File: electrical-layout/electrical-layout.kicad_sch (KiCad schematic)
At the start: 4 parts, among them K1 DNCLEV100, SW1 SW_Push, U1 Outdrive 5.0

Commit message: layout-2025: add cockpit page and schematic
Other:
- added sheet Cockpit (cockpit.kicad_sch)
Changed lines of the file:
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@@
 		(exclude_from_sim no)
 		(at 179.8975 44.7897 0)
-		(size 39.1775 21.2503)
+		(size 37.2725 9.8203)
 		(margins 0.9525 0.9525 0.9525 0.9525)
 		(stroke
@@
 			(project "electrical-layout"
 				(path "/3f5ae950-00dd-4aca-9f75-0d872ff9560e"
+					(page "3")
+				)
+			)
+		)
+	)
+	(sheet
+		(at 174.625 66.675)
+		(size 59.055 19.685)
+		(exclude_from_sim no)
+		(in_bom yes)
+		(on_board yes)
+		(dnp no)
+		(fields_autoplaced yes)
+		(stroke
+			(width 0.1524)
+			(type solid)
+		)
+		(fill
+			(color 0 0 0 0.0000)
+		)
+		(property "Sheetname" "Cockpit"
+			(at 174.625 65.9634 0)
+			(effects
+				(font
+					(size 1.27 1.27)
+				)
+				(justify left bottom)
+			)
+		)
+		(property "Sheetfile" "cockpit.kicad_sch"
+			(at 174.625 86.9446 0)
+			(effects
+				(font
+					(size 1.27 1.27)
+				)
+				(justify left top)
+			)
+		)
+		(instances
+			(project "electrical-layout"
+				(path "/3f5ae950-00dd-4aca-9f75-0d872ff9560e"
 					(page "2")
 				)
@@
 			(project "electrical-layout"
 				(path "/3f5ae950-00dd-4aca-9f75-0d872ff9560e"
-					(page "3")
-				)
-			)
+					(page "4")
+				)
+			)

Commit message: layout-2025: add h2 control page and schematic
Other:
- added sheet H2 Control (h2_control.kicad_sch)
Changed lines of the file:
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@@
+	)
+	(sheet
+		(at 178.435 111.76)
+		(size 60.96 20.955)
+		(exclude_from_sim no)
+		(in_bom yes)
+		(on_board yes)
+		(dnp no)
+		(fields_autoplaced yes)
+		(stroke
+			(width 0.1524)
+			(type solid)
+		)
+		(fill
+			(color 0 0 0 0.0000)
+		)
+		(property "Sheetname" "H2 Control"
+			(at 178.435 111.0484 0)
+			(effects
+				(font
+					(size 1.27 1.27)
+				)
+				(justify left bottom)
+			)
+		)
+		(property "Sheetfile" "h2_control.kicad_sch"
+			(at 178.435 133.2996 0)
+			(effects
+				(font
+					(size 1.27 1.27)
+				)
+				(justify left top)
+			)
+		)
+		(instances
+			(project "electrical-layout"
+				(path "/3f5ae950-00dd-4aca-9f75-0d872ff9560e"
+					(page "5")
+				)
+			)
+		)
 	)
 	(sheet

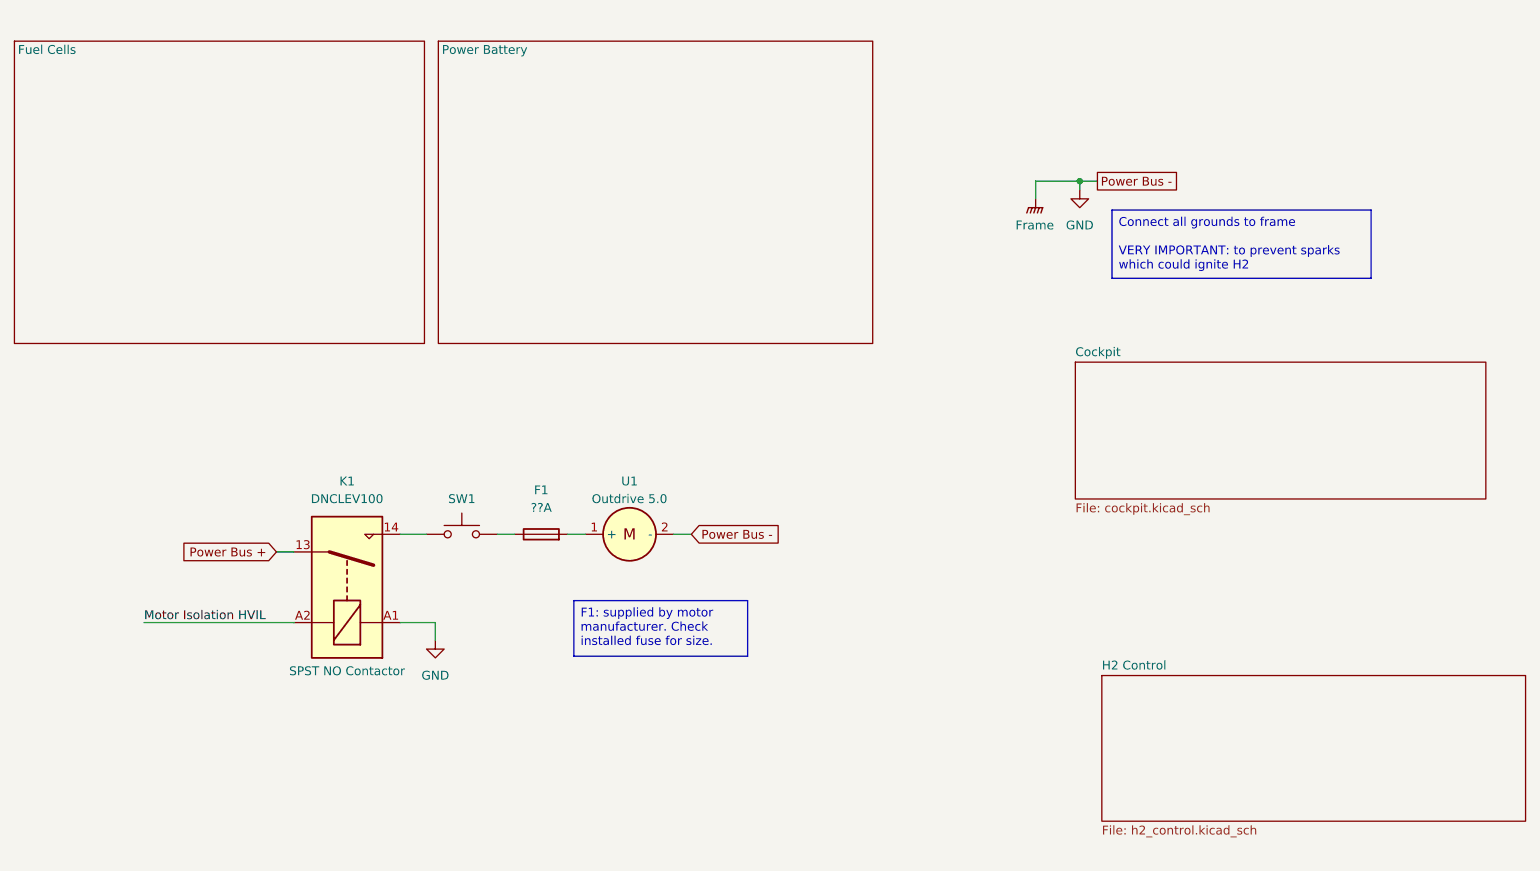
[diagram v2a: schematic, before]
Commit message: layout-2025: reorganize pages
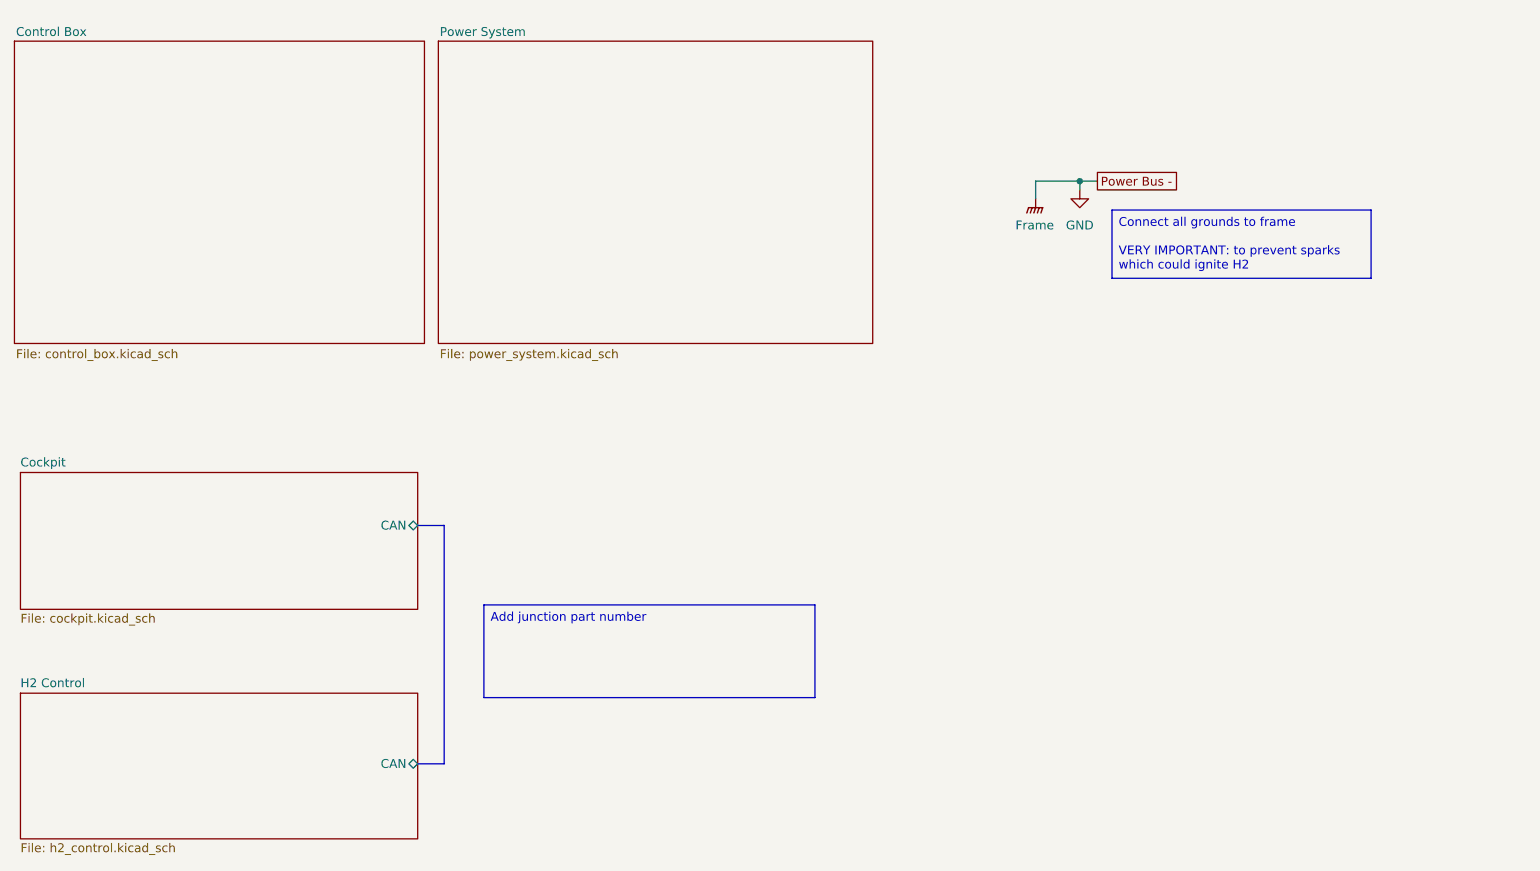
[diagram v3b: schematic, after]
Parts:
- removed F1: ??A, symbol Device:Fuse
- removed K1: DNCLEV100, symbol Relay:Relay_SPST-NO
- removed SW1: SW_Push, symbol Switch:SW_Push
- removed U1: Outdrive 5.0, symbol Exocet:Outboard_5.0
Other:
- sheet Fuel Cells renamed Control Box
- sheet Power Battery renamed Power System
- sheet Cockpit ports: added CAN; removed none
- sheet Control Box: file fuel_cells.kicad_sch -> control_box.kicad_sch
- sheet H2 Control ports: added CAN; removed none
- sheet Power System: file power_battery.kicad_sch -> power_system.kicad_sch

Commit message: layout-2025: add telemetry battery and pcb
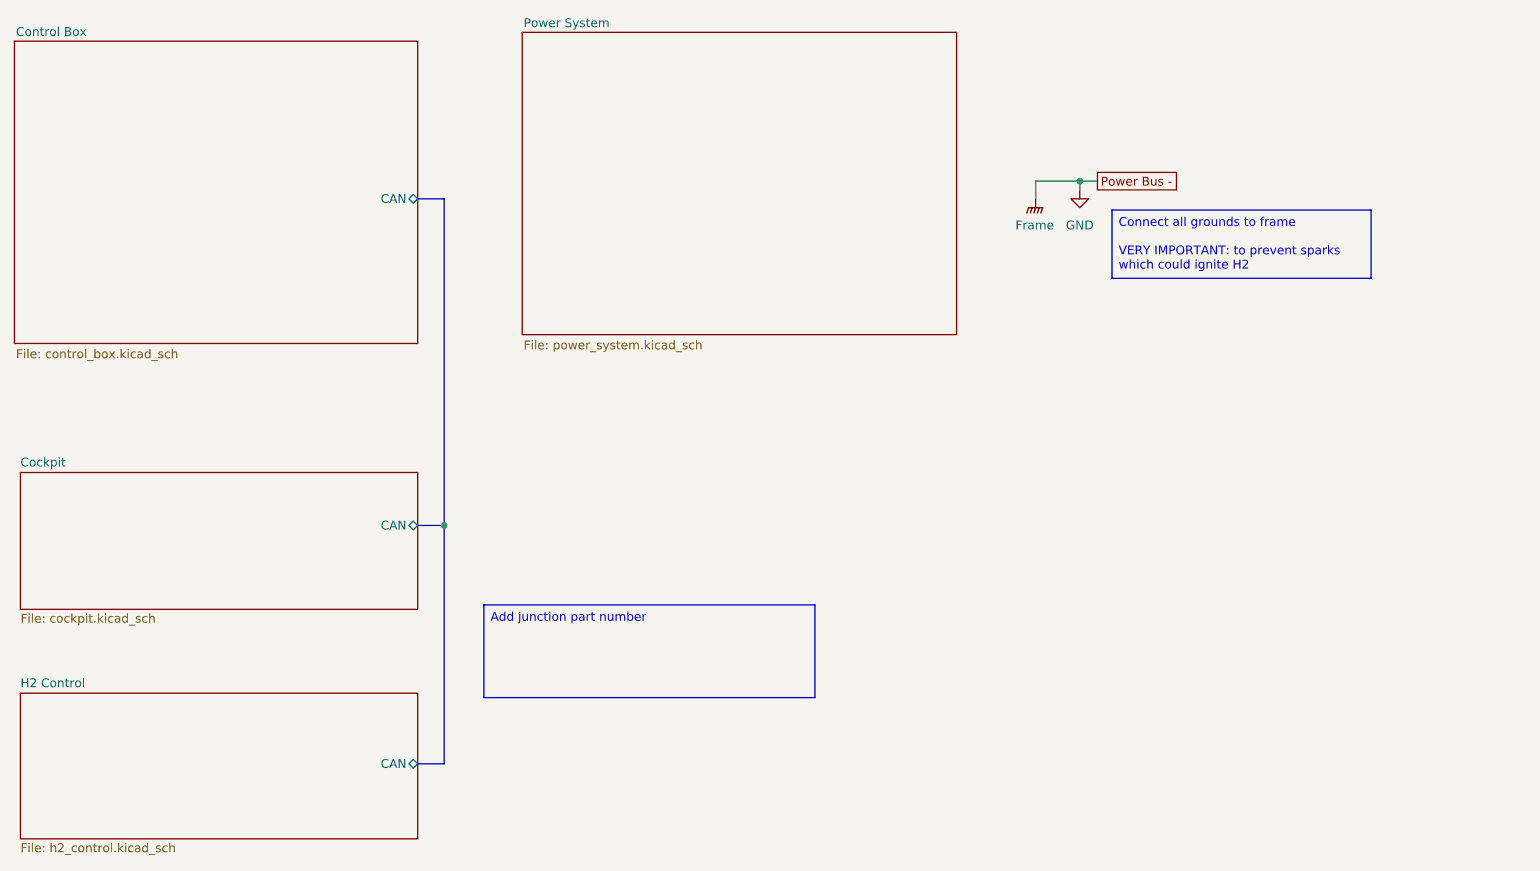
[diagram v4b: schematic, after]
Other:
- sheet Control Box ports: added CAN; removed none
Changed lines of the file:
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@@
 		(color 0 0 0 0)
 	)
+	(junction
+		(at 83.82 90.17)
+		(diameter 0)
+		(color 0 0 0 0)
+	)
+	(bus
+		(pts
+			(xy 80.01 43.18) (xy 83.82 43.18)
+		)
+		(stroke
+			(width 0)
+			(type default)
+		)
+	)
 	(wire
 		(pts
@@
 		(pts
 			(xy 83.82 90.17) (xy 83.82 124.46)
+		)
+		(stroke
+			(width 0)
+			(type default)
+		)
+	)
+	(bus
+		(pts
+			(xy 83.82 43.18) (xy 83.82 90.17)
 		)
 		(stroke
@@
 	(sheet
 		(at 21.9956 20.4959)
-		(size 58.9882 43.4913)
+		(size 58.0144 43.4913)
 		(exclude_from_sim no)
 		(in_bom yes)
@@
 				)
 				(justify left top)
+			)
+		)
+		(pin "CAN" bidirectional
+			(at 80.01 43.18 0)
+			(effects
+				(font
+					(size 1.27 1.27)
+				)
+				(justify right)
 			)
 		)
@@
 	)
 	(sheet
-		(at 82.9834 20.4959)
+		(at 95.0484 19.2259)
 		(size 62.4875 43.4913)
 		(exclude_from_sim no)
@@
 		)
 		(property "Sheetname" "Power System"
-			(at 83.185 18.415 0)
+			(at 95.25 17.145 0)
 			(effects
 				(font
@@
 		)
 		(property "Sheetfile" "power_system.kicad_sch"
-			(at 83.185 64.77 0)
-			(effects
-				(font
+			(at 95.25 63.5 0)
+			(effects
+				(font

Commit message: power-system: add DC-DC charger and temp. switches
This includes changes recommended to us during summer of 2025. Temporary
switch symbols have been used to indicate where to expect them, while
their internal circuit is not yet know and implemented. These will most
likely be replaced by some power transistors in the future.

A few control signals were added and are not yet connected to a control
board, but these shall be implemented on the power control PCB.
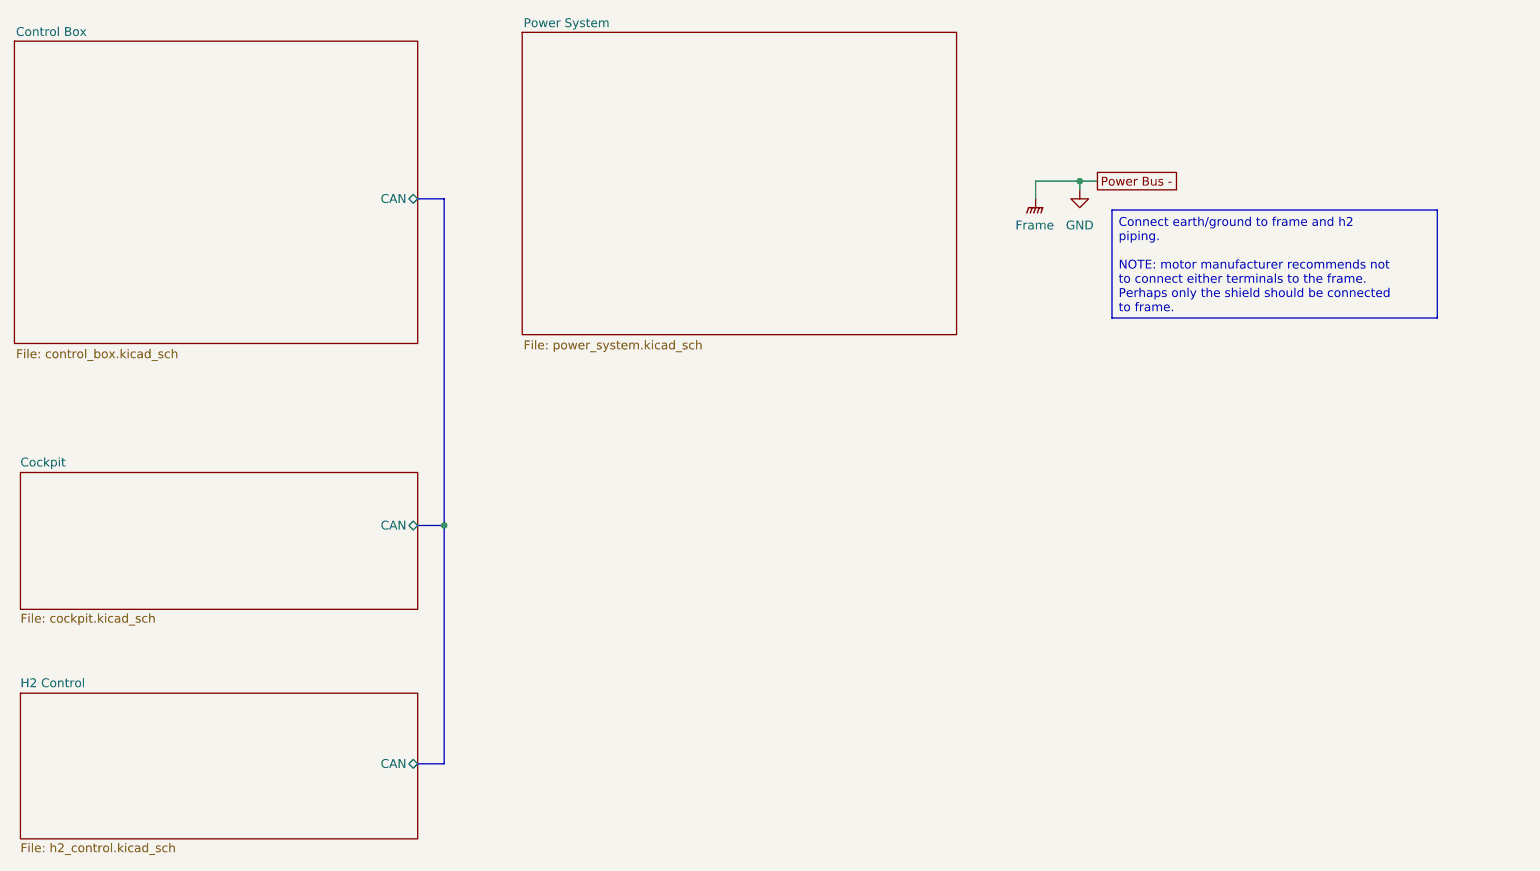
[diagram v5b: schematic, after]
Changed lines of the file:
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@@
 	(title_block
 		(title "Overview")
-		(date "2025-03-15")
-		(rev "v0.2.0")
+		(date "2025-09-06")
+		(rev "v0.3.0")
 	)
-	(text_box "Connect all grounds to frame\n\nVERY IMPORTANT: to prevent sparks which could ignite H2"
+	(text_box "Connect earth/ground to frame and h2 piping.\n\nNOTE: motor manufacturer recommends not to connect either terminals to the frame. Perhaps only the shield should be connected to frame."
 		(exclude_from_sim no)
 		(at 179.8975 44.7897 0)
-		(size 37.2725 9.8203)
+		(size 46.7975 15.5353)
 		(margins 0.9525 0.9525 0.9525 0.9525)
 		(stroke
-			(width 0)
-			(type solid)
-		)
-		(fill
-			(type none)
-		)
-		(effects
-			(font
-				(size 1.27 1.27)
-			)
-			(justify left top)
-		)
-	)
-	(text_box "Add junction part number"
-		(exclude_from_sim no)
-		(at 89.535 101.6 0)
-		(size 47.625 13.335)
-		(margins 0.9525 0.9525 0.9525 0.9525)
-		(stroke

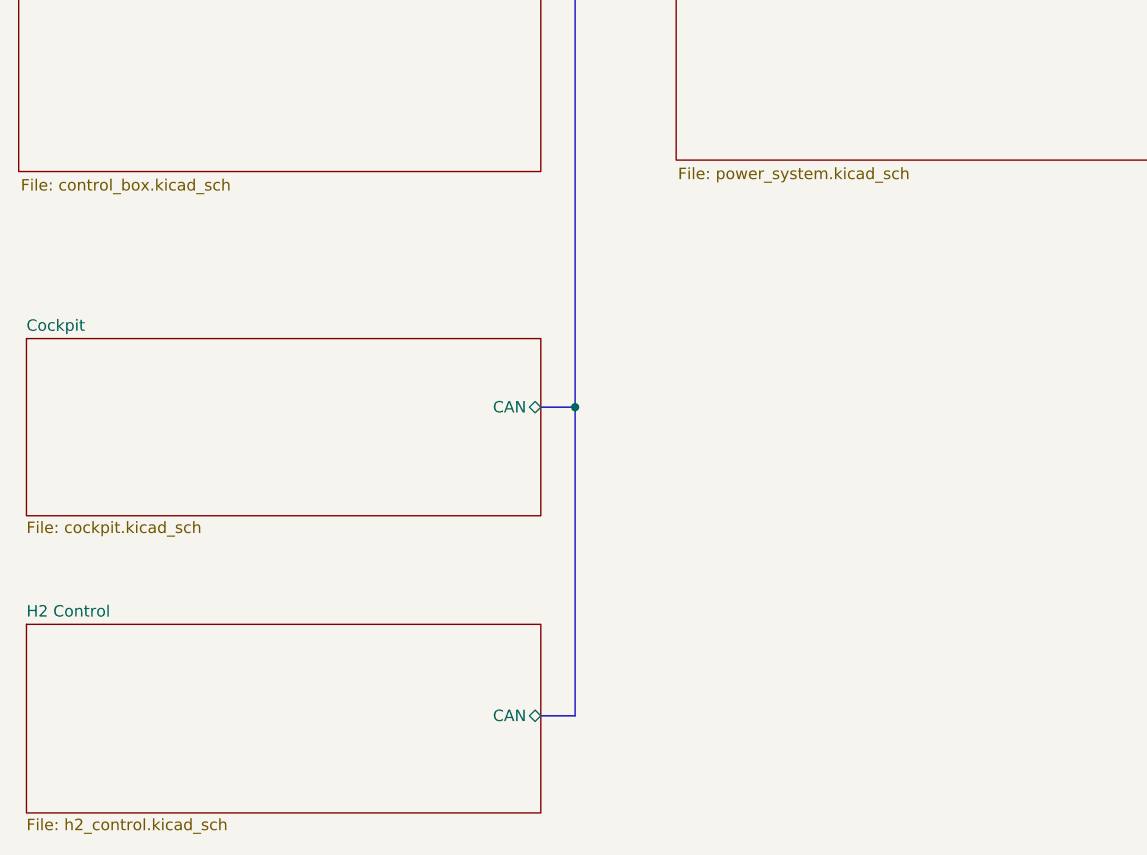
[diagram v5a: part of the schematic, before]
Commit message: layout-2025: change to version 3.0
A few changes were made for this new version:
- Version and dates were changed on all sheets
- Added a switch (temporary symbol) after the telemetry battery
- A few notes were removed, as these have either been resolved or
discussed somewhere else
- Changed battery symbol to multi-cell battery
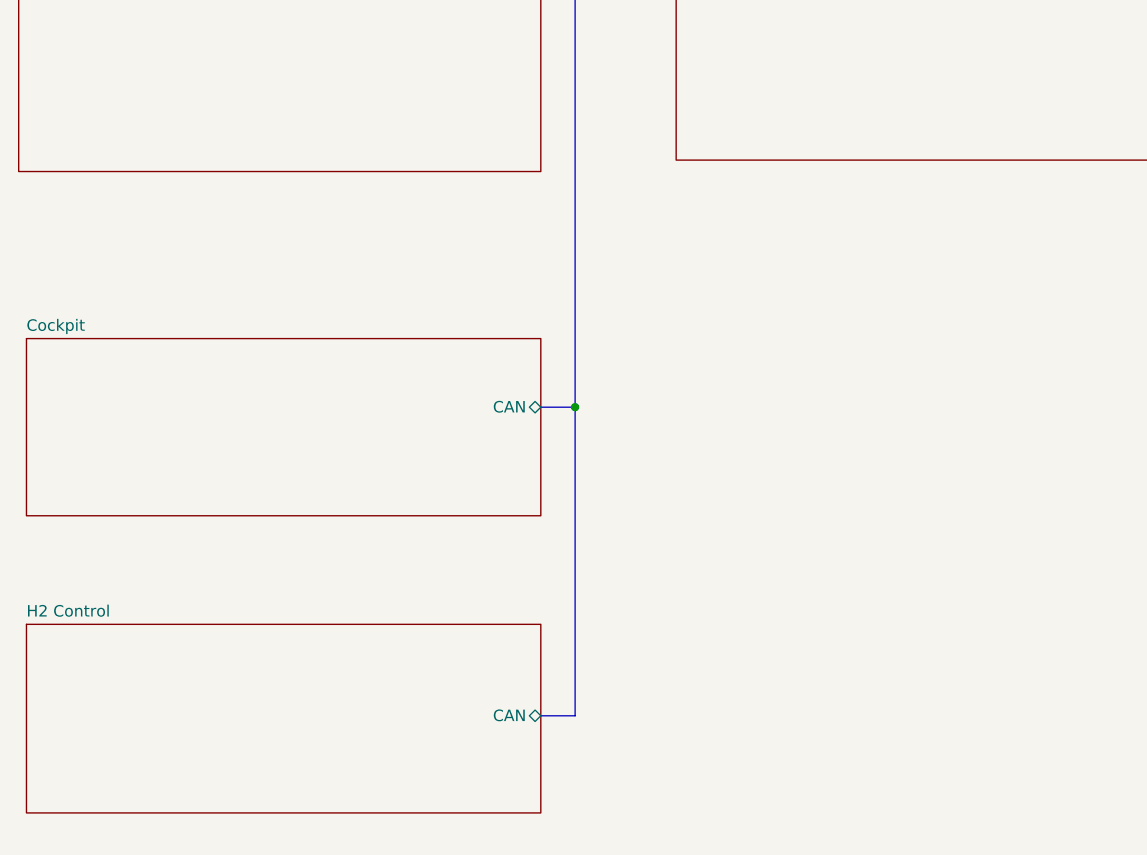
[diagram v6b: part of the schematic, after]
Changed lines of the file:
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@@
 				)
 				(justify left top)
+				(hide yes)
 			)
 		)
@@
 				)
 				(justify left top)
+				(hide yes)
 			)
 		)
@@
 				)
 				(justify left top)
+				(hide yes)
 			)
 		)
@@
 				)
 				(justify left top)
+				(hide yes)
 			)
 		)
